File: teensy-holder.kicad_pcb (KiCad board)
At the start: 2 copper layers, 5 parts, among them P1 BNC, U1 Teensy3.2_DIP

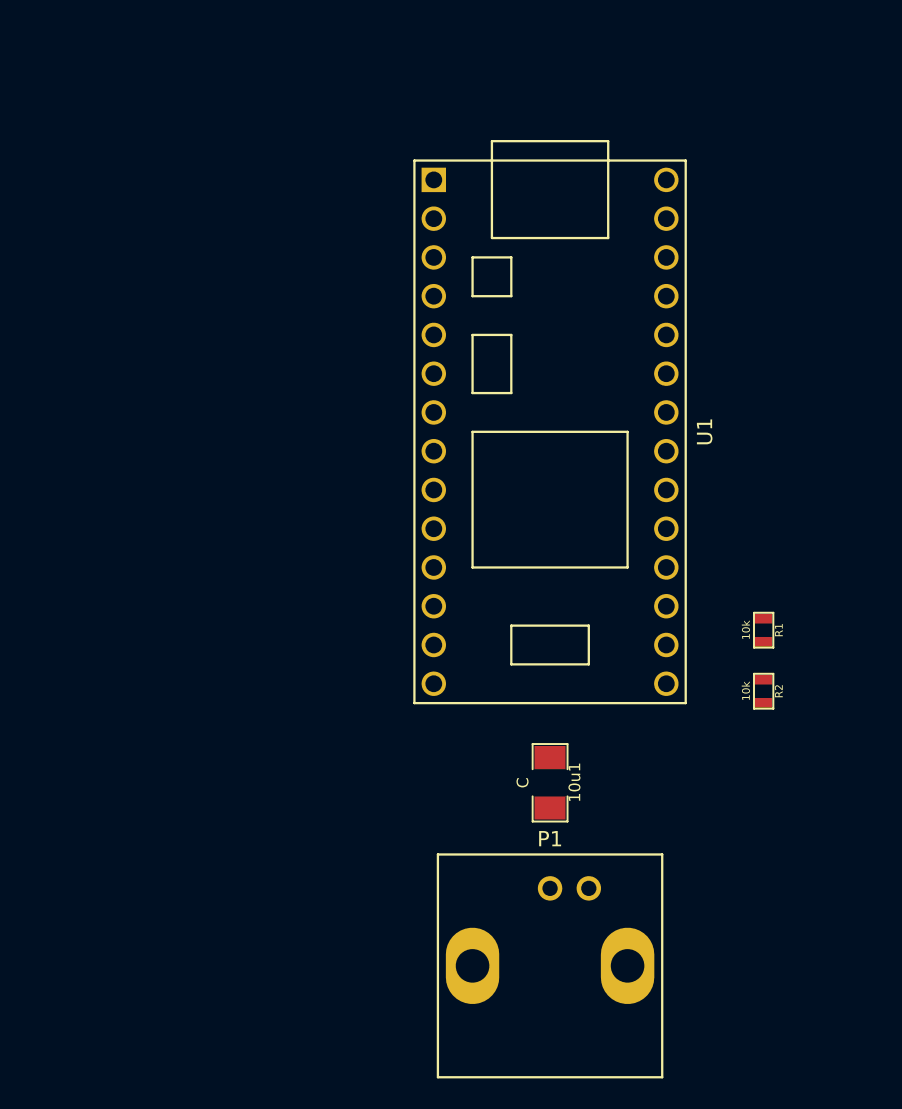
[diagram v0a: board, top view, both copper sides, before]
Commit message: Added more parts, started board layout
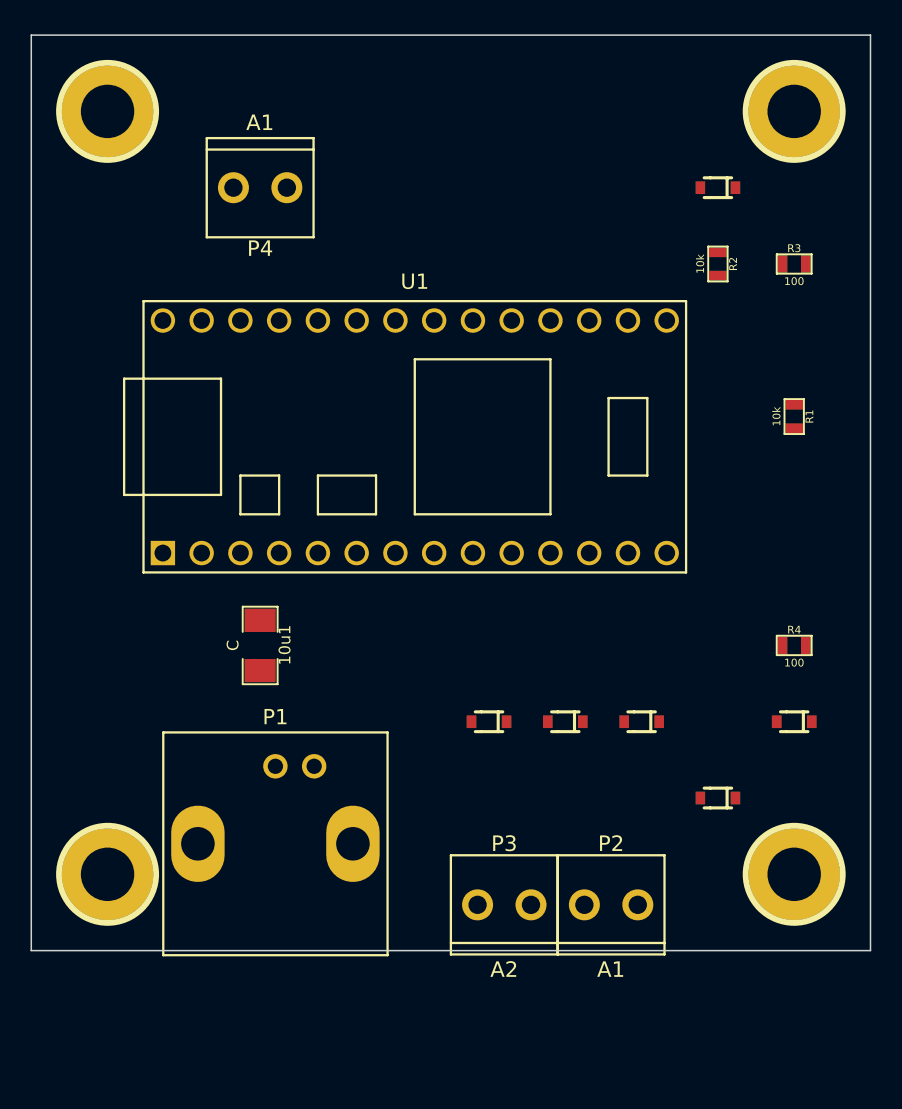
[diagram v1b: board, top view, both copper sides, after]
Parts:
- added D1: D, visgence_parts:SOD-323, F.Cu at (75.0, 45.0)
- added D2: D, visgence_parts:SOD-323, F.Cu at (80.0, 80.0)
- added D3: D, visgence_parts:SOD-323, F.Cu at (75.0, 85.0)
- added D4: D, visgence_parts:SOD-323, F.Cu at (70.0, 80.0)
- added D5: D, visgence_parts:SOD-323, F.Cu at (60.0, 80.0)
- added D6: D, visgence_parts:SOD-323, F.Cu at (65.0, 80.0)
- added P2: A1, visgence_parts:Term3.5-2, F.Cu at (68.0, 92.0)
- added P3: A2, visgence_parts:Term3.5-2, F.Cu at (61.0, 92.0)
- added P4: A1, visgence_parts:Term3.5-2, F.Cu at (45.0, 45.0)
- added R3: 100, visgence_parts:SM0603_VIS, F.Cu at (80.0, 50.0)
- added R4: 100, visgence_parts:SM0603_VIS, F.Cu at (80.0, 75.0)
- added h?: pin, visgence_parts:1pin_C, F.Cu at (35.0, 40.0)
- added h?: pin, visgence_parts:1pin_C, F.Cu at (80.0, 40.0)
- added h?: pin, visgence_parts:1pin_C, F.Cu at (80.0, 90.0)
- added h?: pin, visgence_parts:1pin_C, F.Cu at (35.0, 90.0)
- moved R2 28.2 mm to (75.0, 50.0)
- moved 10u1 21.0 mm to (45.0, 75.0)
- moved P1 19.7 mm to (46.0, 88.0)
- moved R1 14.1 mm to (80.0, 60.0)
- moved U1 8.87 mm to (55.1, 61.3), turned to 0 degrees
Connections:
- net Net-(10u1-Pad1) renamed A0
- net Net-(U1-Pad10) renamed SS1
- net Net-(U1-Pad11) renamed MOSI
- net Net-(U1-Pad12) renamed MISO
- net Net-(U1-Pad13) renamed SCK
- net Net-(U1-Pad9) renamed SS0
- U1 pad 15: Net-(U1-Pad15) -> A1
- U1 pad 16: Net-(U1-Pad16) -> A2
- U1 pad vin: Net-(U1-Padvin) -> VIN
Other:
- board outline added: 55 x 60 mm

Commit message: board layout
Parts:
- D1, D2, D3, D4, D5, D6: footprint visgence_parts:SOD-323 -> Diodes_SMD:D_SOD-323_HandSoldering
- moved R3 49.2 mm to (44.5, 84.0), turned to 90 degrees
- moved D1 46.5 mm to (40.2, 75.8)
- moved D2 30.0 mm to (50.5, 74.8), turned to 180 degrees
- moved R4 29.9 mm to (51.5, 84.0), turned to 90 degrees
- moved D4 24.8 mm to (45.4, 77.2)
- moved 10u1 20.0 mm to (65.0, 75.2), turned to 180 degrees
- moved D6 19.0 mm to (46.0, 80.5)
- moved P2 18.4 mm to (49.8, 90.0)
- moved P3 18.4 mm to (42.8, 90.0)
- moved D5 18.3 mm to (41.8, 80.5)
- moved R1 18.1 mm to (66.5, 48.0), turned to 0 degrees
- moved P1 17.4 mm to (63.2, 86.0)
- moved D3 11.2 mm to (72.0, 74.2)
- moved P4 11.2 mm to (55.0, 40.0)
- moved R2 5.62 mm to (69.8, 48.0), turned to 0 degrees
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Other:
- board size 55 x 60 mm -> 46.5 x 56.5 mm

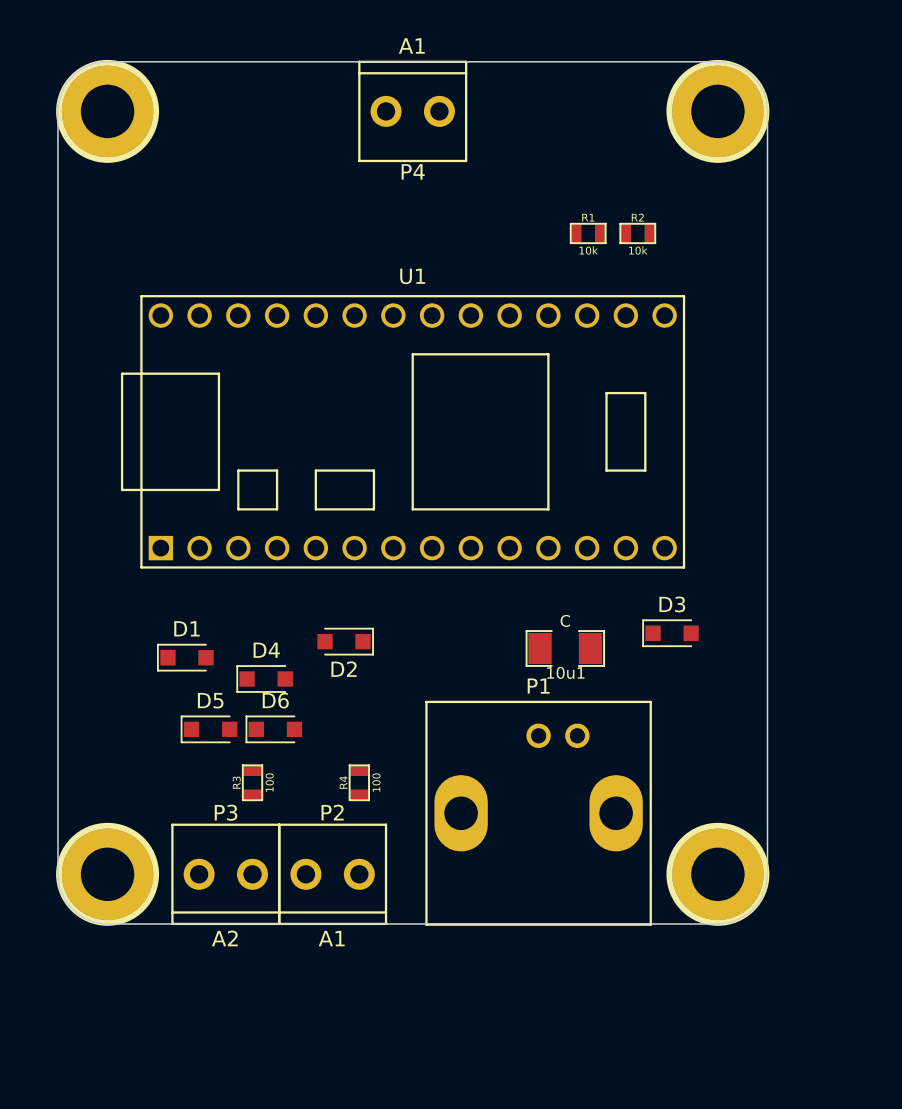
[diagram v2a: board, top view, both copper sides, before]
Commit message: Added 3.3v to term at bottom
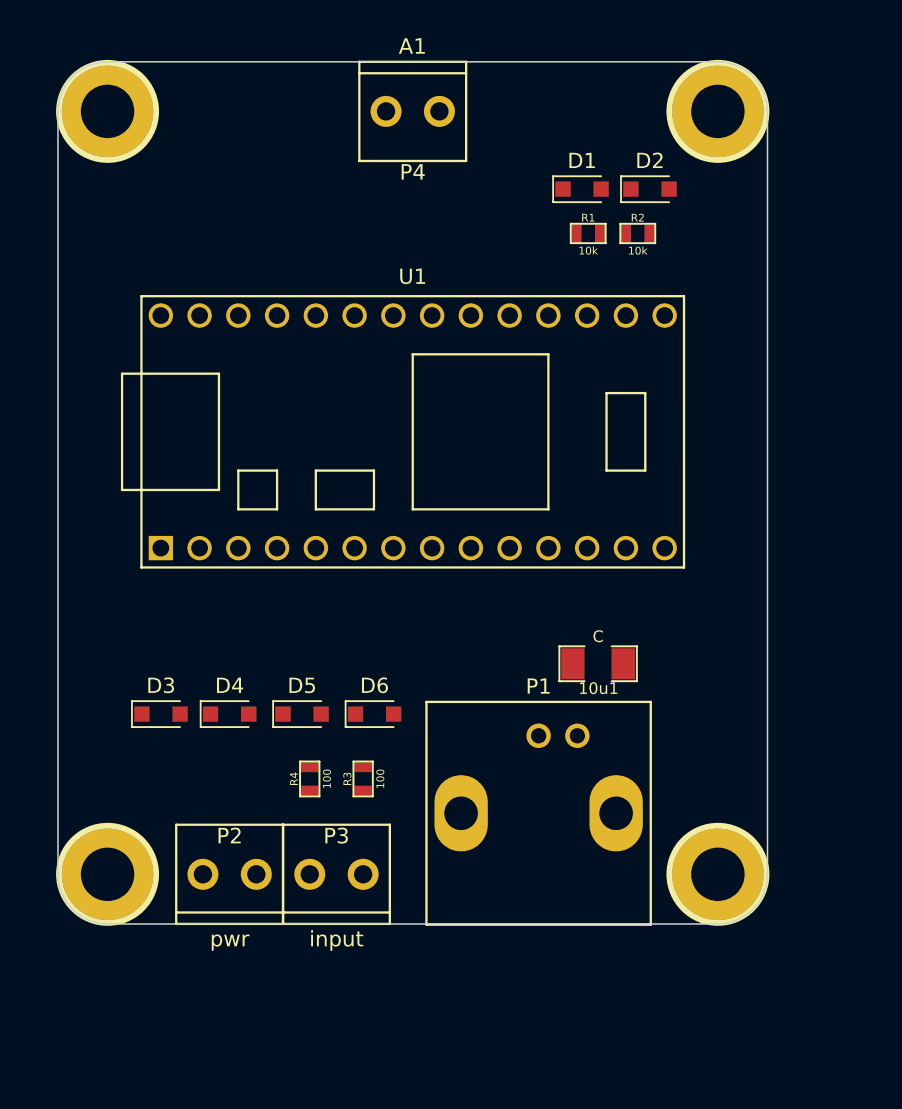
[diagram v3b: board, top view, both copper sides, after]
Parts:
- P2: value A1 -> pwr
- P3: value A2 -> input
- moved D1 40.2 mm to (66.1, 45.1)
- moved D2 35.8 mm to (70.5, 45.1), turned to 0 degrees
- moved D3 33.9 mm to (38.5, 79.5)
- moved R3 7.25 mm to (51.8, 83.8)
- moved P3 7.25 mm to (50.0, 90.0)
- moved P2 6.75 mm to (43.0, 90.0)
- moved D6 6.58 mm to (52.5, 79.5)
- moved D5 6.08 mm to (47.8, 79.5)
- moved D4 3.32 mm to (43.0, 79.5)
- moved R4 3.26 mm to (48.2, 83.8)
- moved 10u1 2.37 mm to (67.2, 76.2)
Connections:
- P2 pad 2: Net-(P2-Pad2) -> +3V3
- P3 pad 1: GND -> Net-(P3-Pad1)
- R4 pad 1: Net-(P2-Pad2) -> Net-(P3-Pad1)
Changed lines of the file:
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@@
   (net 22 A1)
   (net 23 A2)
-  (net 24 "Net-(P2-Pad2)")
-  (net 25 "Net-(P3-Pad2)")
-  (net 26 VIN)
-  (net 27 SCK)
-  (net 28 MISO)
-  (net 29 MOSI)
-  (net 30 SS1)
-  (net 31 SS0)
+  (net 24 "Net-(P3-Pad2)")
+  (net 25 VIN)
+  (net 26 SCK)
+  (net 27 MISO)
+  (net 28 MOSI)
+  (net 29 SS1)
+  (net 30 SS0)
+  (net 31 "Net-(P3-Pad1)")
   (net_class Default "This is the default net class."
     (clearance 0.2)
@@
     (add_net MOSI)
     (add_net "Net-(10u1-Pad2)")
-    (add_net "Net-(P2-Pad2)")
+    (add_net "Net-(P3-Pad1)")
     (add_net "Net-(P3-Pad2)")
     (add_net "Net-(U1-Pad0)")
@@
   )
   (module visgence_parts:SM1206_VIS (layer F.Cu)
-    (at 65 75.2 180)
+    (at 67.15 76.2 180)
     (attr smd)
     (fp_text reference 10u1 (at -0.0254 -1.6256 180) (layer F.SilkS)
@@
     (fp_line (start -17.78 8.89) (end -17.78 -8.89) (layer F.SilkS) (width 0.15))
     (pad 13 thru_hole circle (at 16.51 -7.62) (size 1.6 1.6) (drill 1.1) (layers *.Cu *.Mask F.SilkS)
-      (net 27 SCK))
+      (net 26 SCK))
     (pad 12 thru_hole circle (at 16.51 7.62) (size 1.6 1.6) (drill 1.1) (layers *.Cu *.Mask F.SilkS)
-      (net 28 MISO))
+      (net 27 MISO))
     (pad 14 thru_hole circle (at 13.97 -7.62) (size 1.6 1.6) (drill 1.1) (layers *.Cu *.Mask F.SilkS)
       (net 21 A0))
@@
       (net 11 "Net-(U1-Padagnd)"))
     (pad vin thru_hole circle (at -16.51 -7.62) (size 1.6 1.6) (drill 1.1) (layers *.Cu *.Mask F.SilkS)
-      (net 26 VIN))
+      (net 25 VIN))
     (pad 11 thru_hole circle (at 13.97 7.62) (size 1.6 1.6) (drill 1.1) (layers *.Cu *.Mask F.SilkS)
-      (net 29 MOSI))
+      (net 28 MOSI))
     (pad 10 thru_hole circle (at 11.43 7.62) (size 1.6 1.6) (drill 1.1) (layers *.Cu *.Mask F.SilkS)
-      (net 30 SS1))
+      (net 29 SS1))
     (pad 9 thru_hole circle (at 8.89 7.62) (size 1.6 1.6) (drill 1.1) (layers *.Cu *.Mask F.SilkS)
-      (net 31 SS0))
+      (net 30 SS0))
     (pad 8 thru_hole circle (at 6.35 7.62) (size 1.6 1.6) (drill 1.1) (layers *.Cu *.Mask F.SilkS)
       (net 12 "Net-(U1-Pad8)"))
@@
   )
   (module visgence_parts:Term3.5-2 (layer F.Cu)
-    (at 49.75 90)
-    (fp_text reference P2 (at 0 -4) (layer F.SilkS)
+    (at 43 90)
+    (fp_text reference P2 (at 0 -2.5) (layer F.SilkS)
       (effects (font (size 1.016 1.016) (thickness 0.127)))
     )
-    (fp_text value A1 (at 0 4.24942) (layer F.SilkS)
+    (fp_text value pwr (at 0 4.24942) (layer F.SilkS)
       (effects (font (size 1.016 1.016) (thickness 0.127)))
     )
@@
       (net 2 GND))
     (pad 2 thru_hole circle (at 1.75006 0) (size 2.032 2.032) (drill 1.2) (layers *.Cu *.Mask)
-      (net 24 "Net-(P2-Pad2)"))
+      (net 3 +3V3))
   )
   (module visgence_parts:Term3.5-2 (layer F.Cu)
-    (at 42.75 90)
-    (fp_text reference P3 (at 0 -4) (layer F.SilkS)
+    (at 50 90)
+    (fp_text reference P3 (at 0 -2.5) (layer F.SilkS)
       (effects (font (size 1.016 1.016) (thickness 0.127)))
     )
-    (fp_text value A2 (at 0 4.24942) (layer F.SilkS)
+    (fp_text value input (at 0 4.24942) (layer F.SilkS)
       (effects (font (size 1.016 1.016) (thickness 0.127)))
     )
@@
     (fp_line (start -3.5 3.25) (end -3.5 -3.25) (layer F.SilkS) (width 0.15))
     (pad 1 thru_hole circle (at -1.75006 0) (size 2.032 2.032) (drill 1.2) (layers *.Cu *.Mask)
-      (net 2 GND))
+      (net 31 "Net-(P3-Pad1)"))
     (pad 2 thru_hole circle (at 1.75006 0) (size 2.032 2.032) (drill 1.2) (layers *.Cu *.Mask)
-      (net 25 "Net-(P3-Pad2)"))
+      (net 24 "Net-(P3-Pad2)"))
   )
   (module visgence_parts:Term3.5-2 (layer F.Cu)
@@
       (net 2 GND))
     (pad 2 thru_hole circle (at 1.75006 0 180) (size 2.032 2.032) (drill 1.2) (layers *.Cu *.Mask)
-      (net 26 VIN))
+      (net 25 VIN))
   )
   (module visgence_parts:SM0603_VIS (layer F.Cu)
-    (at 44.5 84 90)
+    (at 51.75 83.75 90)
     (attr smd)
     (fp_text reference R3 (at 0 -1.016 90) (layer F.SilkS)
@@
     (fp_line (start -1.143 0.635) (end -1.143 -0.635) (layer F.SilkS) (width 0.127))
     (pad 1 smd rect (at -0.762 0 90) (size 0.635 1.143) (layers F.Cu F.Paste F.Mask)
-      (net 25 "Net-(P3-Pad2)"))
+      (net 24 "Net-(P3-Pad2)"))
     (pad 2 smd rect (at 0.762 0 90) (size 0.635 1.143) (layers F.Cu F.Paste F.Mask)
       (net 23 A2))
@@
   )
   (module visgence_parts:SM0603_VIS (layer F.Cu)
-    (at 51.5 84 90)
+    (at 48.25 83.75 90)
     (attr smd)
     (fp_text reference R4 (at 0 -1.016 90) (layer F.SilkS)
@@
     (fp_line (start -1.143 0.635) (end -1.143 -0.635) (layer F.SilkS) (width 0.127))
     (pad 1 smd rect (at -0.762 0 90) (size 0.635 1.143) (layers F.Cu F.Paste F.Mask)
-      (net 24 "Net-(P2-Pad2)"))
+      (net 31 "Net-(P3-Pad1)"))
     (pad 2 smd rect (at 0.762 0 90) (size 0.635 1.143) (layers F.Cu F.Paste F.Mask)
       (net 22 A1))
@@
   )
   (module Diodes_SMD:D_SOD-323_HandSoldering (layer F.Cu)
-    (at 40.2 75.8)
+    (at 66.1 45.1)
     (descr SOD-323)
     (tags SOD-323)
@@
   )
   (module Diodes_SMD:D_SOD-323_HandSoldering (layer F.Cu)
-    (at 50.5 74.75 180)
+    (at 70.55 45.1)
     (descr SOD-323)
     (tags SOD-323)
     (attr smd)
-    (fp_text reference D2 (at 0 -1.85 180) (layer F.SilkS)
-      (effects (font (size 1 1) (thickness 0.15)))
-    )
-    (fp_text value D (at 0.1 1.9 180) (layer F.Fab)
+    (fp_text reference D2 (at 0 -1.85) (layer F.SilkS)
+      (effects (font (size 1 1) (thickness 0.15)))
+    )
+    (fp_text value D (at 0.1 1.9) (layer F.Fab)
       (effects (font (size 1 1) (thickness 0.15)))
     )
@@
     (fp_line (start -1.9 0.85) (end 1.25 0.85) (layer F.SilkS) (width 0.12))
     (fp_line (start -1.9 -0.85) (end 1.25 -0.85) (layer F.SilkS) (width 0.12))
-    (pad 1 smd rect (at -1.25 0 180) (size 1 1) (layers F.Cu F.Paste F.Mask)
+    (pad 1 smd rect (at -1.25 0) (size 1 1) (layers F.Cu F.Paste F.Mask)
       (net 21 A0))
-    (pad 2 smd rect (at 1.25 0 180) (size 1 1) (layers F.Cu F.Paste F.Mask)
+    (pad 2 smd rect (at 1.25 0) (size 1 1) (layers F.Cu F.Paste F.Mask)
       (net 2 GND))
     (model Diodes_SMD.3dshapes/D_SOD-323.wrl
@@
   )
   (module Diodes_SMD:D_SOD-323_HandSoldering (layer F.Cu)
-    (at 72 74.2)
+    (at 38.5 79.5)
     (descr SOD-323)
     (tags SOD-323)
@@
   )
   (module Diodes_SMD:D_SOD-323_HandSoldering (layer F.Cu)
-    (at 45.4 77.2)
+    (at 43 79.5)
     (descr SOD-323)
     (tags SOD-323)
@@
   )
   (module Diodes_SMD:D_SOD-323_HandSoldering (layer F.Cu)
-    (at 41.75 80.5)
+    (at 47.75 79.5)
     (descr SOD-323)
     (tags SOD-323)
@@
   )
   (module Diodes_SMD:D_SOD-323_HandSoldering (layer F.Cu)
-    (at 46 80.5)
+    (at 52.5 79.5)
     (descr SOD-323)
     (tags SOD-323)

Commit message: Added more ports, did some layout, swaped diodes
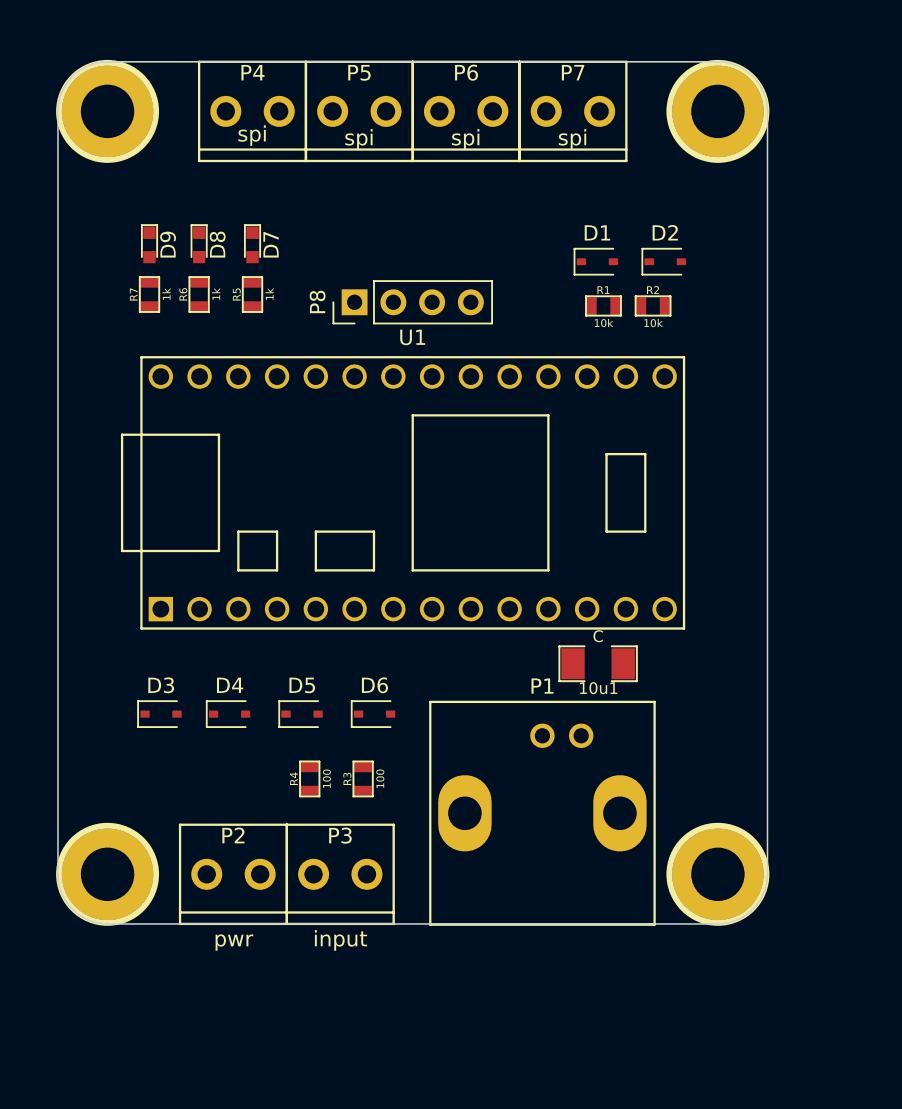
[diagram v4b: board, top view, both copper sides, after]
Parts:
- added D7: RED, LEDs:LED_0603, F.Cu at (44.5, 48.8)
- added D8: GREEN, LEDs:LED_0603, F.Cu at (41.0, 48.8)
- added D9: BLUE, LEDs:LED_0603, F.Cu at (37.8, 48.8)
- added P5: spi, visgence_parts:Term3.5-2, F.Cu at (51.5, 40.0)
- added P6: spi, visgence_parts:Term3.5-2, F.Cu at (58.5, 40.0)
- added P7: spi, visgence_parts:Term3.5-2, F.Cu at (65.5, 40.0)
- added P8: i2c, Pin_Headers:Pin_Header_Straight_1x04_Pitch2.54mm, F.Cu at (51.2, 52.5)
- added R5: 1k, visgence_parts:SM0603_VIS, F.Cu at (44.5, 52.0)
- added R6: 1k, visgence_parts:SM0603_VIS, F.Cu at (41.0, 52.0)
- added R7: 1k, visgence_parts:SM0603_VIS, F.Cu at (37.8, 52.0)
- D1, D2, D3, D4, D5, D6: footprint Diodes_SMD:D_SOD-323_HandSoldering -> Diodes_SMD:D_SOD-323
- P4: value A1 -> spi
- moved P4 10.5 mm to (44.5, 40.0), turned to 0 degrees
- moved D1 4.85 mm to (67.1, 49.9)
- moved D2 4.85 mm to (71.5, 49.9)
- moved R1 4.85 mm to (67.5, 52.8)
- moved R2 4.85 mm to (70.8, 52.8)
- moved U1 4.00 mm to (55.0, 65.0)
- moved P1 0.25 mm to (63.5, 86.0)
- moved P2 0.25 mm to (43.2, 90.0)
- moved P3 0.25 mm to (50.2, 90.0)
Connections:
- U1 pad 10: SS1 -> D10
- U1 pad 18: Net-(U1-Pad18) -> SDA
- U1 pad 19: Net-(U1-Pad19) -> SCL
- U1 pad 21: Net-(U1-Pad21) -> LED1
- U1 pad 22: Net-(U1-Pad22) -> LED2
- U1 pad 23: Net-(U1-Pad23) -> LED3
- U1 pad 9: SS0 -> D9
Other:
- net class Default: trace_width 0.25 -> 0.625
